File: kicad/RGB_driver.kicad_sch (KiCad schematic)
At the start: 17 parts, among them J2 USB_C_Receptacle_USB2.0_16P, SW2 SW_Push_Open_Dual, SW4 SW_Push_Open_Dual, U3 ATtiny85-20P

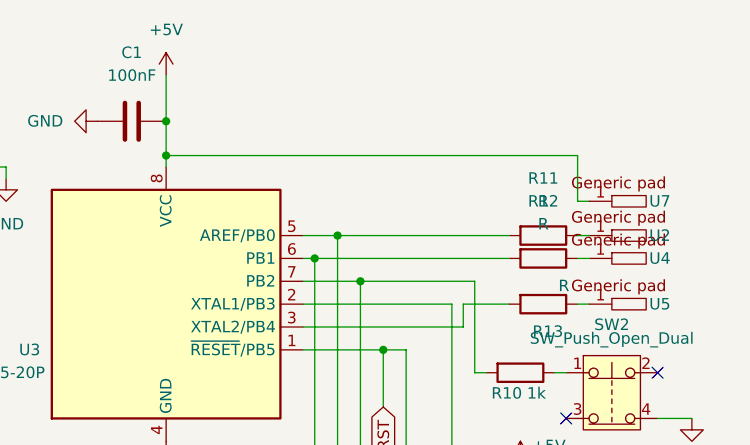
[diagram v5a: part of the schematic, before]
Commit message: change: external power pad changed to a passive connector, new gerber files
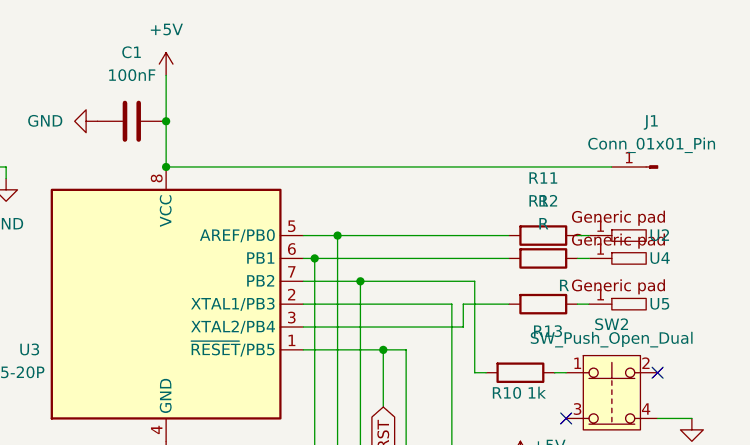
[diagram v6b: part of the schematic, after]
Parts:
- removed U7: ~, footprint_radiocontorler:simple_generic_pad, symbol Amplifier_Operational:generic_pad
- added J1: Conn_01x01_Pin, footprint_radiocontorler:simple_generic_pad, symbol Connector:Conn_01x01_Pin
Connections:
- net +5V: now also J1.1 (Pin_1)
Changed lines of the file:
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@@
 	)
 	(junction
-		(at 107.95 57.15)
+		(at 107.95 58.42)
 		(diameter 0)
 		(color 0 0 0 0)
@@
 	(wire
 		(pts
-			(xy 107.95 57.15) (xy 107.95 58.42)
-		)
-		(stroke
-			(width 0)
-			(type default)
-		)
-	)
-	(wire
-		(pts
 			(xy 124.46 68.58) (xy 124.46 106.68)
 		)
@@
 	(wire
 		(pts
+			(xy 107.95 58.42) (xy 157.48 58.42)
+		)
+		(stroke
+			(width 0)
+			(type default)
+		)
+	)
+	(wire
+		(pts
 			(xy 67.31 111.76) (xy 67.31 114.3)
 		)
@@
 	(wire
 		(pts
-			(xy 153.67 62.23) (xy 154.94 62.23)
-		)
-		(stroke
-			(width 0)
-			(type default)
-		)
-	)
-	(wire
-		(pts
 			(xy 127 66.04) (xy 146.05 66.04)
 		)
@@
 	(wire
 		(pts
+			(xy 107.95 53.34) (xy 107.95 58.42)
+		)
+		(stroke
+			(width 0)
+			(type default)
+		)
+	)
+	(wire
+		(pts
 			(xy 143.51 96.52) (xy 139.7 96.52)
 		)
@@
 	(wire
 		(pts
-			(xy 107.95 57.15) (xy 153.67 57.15)
-		)
-		(stroke
-			(width 0)
-			(type default)
-		)
-	)
-	(wire
-		(pts
 			(xy 77.47 53.34) (xy 77.47 48.26)
 		)
@@
 	(wire
 		(pts
-			(xy 153.67 57.15) (xy 153.67 62.23)
-		)
-		(stroke
-			(width 0)
-			(type default)
-		)
-	)
-	(wire
-		(pts
 			(xy 153.67 73.66) (xy 154.94 73.66)
 		)
@@
 		(pts
 			(xy 146.05 73.66) (xy 140.97 73.66)
-		)
-		(stroke
-			(width 0)
-			(type default)
-		)
-	)
-	(wire
-		(pts
-			(xy 107.95 53.34) (xy 107.95 57.15)
 		)
 		(stroke
@@
 	)
 	(symbol
+		(lib_id "Connector:Conn_01x01_Pin")
+		(at 162.56 58.42 180)
+		(unit 1)
+		(exclude_from_sim no)
+		(in_bom yes)
+		(on_board yes)
+		(dnp no)
+		(fields_autoplaced yes)
+		(property "Reference" "J1"
+			(at 161.925 53.34 0)
+			(effects
+				(font
+					(size 1.27 1.27)
+				)
+			)
+		)
+		(property "Value" "Conn_01x01_Pin"
+			(at 161.925 55.88 0)
+			(effects
+				(font
+					(size 1.27 1.27)
+				)
+			)
+		)
+		(property "Footprint" "footprint_radiocontorler:simple_generic_pad"
+			(at 162.56 58.42 0)
+			(effects
+				(font
+					(size 1.27 1.27)
+				)
+				(hide yes)
+			)
+		)
+		(property "Datasheet" "~"
+			(at 162.56 58.42 0)
+			(effects
+				(font
+					(size 1.27 1.27)
+				)
+				(hide yes)
+			)
+		)
+		(property "Description" "Generic connector, single row, 01x01, script generated"
+			(at 162.56 58.42 0)
+			(effects
+				(font
+					(size 1.27 1.27)
+				)
+				(hide yes)
+			)
+		)
+		(pin "1"
+		)
+		(instances
+			(project ""
+				(path "/1ccb5a9c-254c-4919-974f-8891fcdc32e1"
+					(reference "J1")
+					(unit 1)
+				)
+			)
+		)
+	)
+	(symbol
 		(lib_id "Device:R")
 		(at 149.86 66.04 270)
@@
 					(unit 1)
 				)
-			)
-		)
-	)
-	(symbol
-		(lib_id "Amplifier_Operational:generic_pad")
-		(at 158.75 62.23 0)
-		(unit 1)
-		(exclude_from_sim no)
-		(in_bom yes)
-		(on_board yes)
-		(dnp no)
-		(property "Reference" "U7"
-			(at 162.814 62.23 0)
-			(effects
-				(font
-					(size 1.27 1.27)
-				)
-			)
-		)
-		(property "Value" "~"
-			(at 158.242 57.15 0)
-			(effects
-				(font
-					(size 1.27 1.27)
-				)
-			)
-		)
-		(property "Footprint" "footprint_radiocontorler:simple_generic_pad"
-			(at 158.75 62.23 0)
-			(effects
-				(font
-					(size 1.27 1.27)
-				)
-				(hide yes)
-			)
-		)
-		(property "Datasheet" ""
-			(at 158.75 62.23 0)
-			(effects
-				(font
-					(size 1.27 1.27)
-				)
-				(hide yes)
-			)
-		)
-		(property "Description" ""
-			(at 158.75 62.23 0)
-			(effects
-				(font
-					(size 1.27 1.27)
-				)
-				(hide yes)
-			)
-		)
-		(pin "1"
-		)
-		(instances
-			(project "RGB_driver"
-				(path "/1ccb5a9c-254c-4919-974f-8891fcdc32e1"
-					(reference "U7")
-					(unit 1)
-				)
